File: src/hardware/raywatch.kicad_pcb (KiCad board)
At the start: 2 copper layers, 388 parts, among them J1 Conn_01x02_Pin, J10 Conn_01x04_Pin, J11 Conn_01x04_Pin, J12 Conn_01x02_Pin, J13 Conn_01x02_Pin, J14 Conn_02x08_Top_Bottom, J15 Conn_02x08_Top_Bottom, J16 Conn_02x08_Top_Bottom, J17 Conn_02x08_Top_Bottom, J18 Conn_01x02_Pin, J19 Conn_01x02_Pin, J2 Conn_01x02_Pin, J20 Conn_01x02_Pin, J21 Conn_02x08_Top_Bottom, J22 Conn_01x02_Pin, J23 Conn_01x04_Pin, J24 Conn_01x02_Pin, J25 Conn_01x02_Pin, J26 Conn_01x02_Pin, J27 Conn_01x01_Pin, J28 Conn_01x01_Pin, J29 Conn_01x02_Pin, J3 Conn_01x02_Pin, J30 Conn_01x04_Pin, J31 Conn_01x04_Pin, J32 Conn_01x01_Pin, J33 Conn_01x01_Pin, J34 046809612110846+, J35 Conn_01x02_Pin, J36 Conn_01x02_Pin, J37 Conn_01x02_Pin, J38 Conn_01x02_Pin, J39 Conn_01x02_Pin, J4 Conn_01x02_Pin, J40 Conn_01x02_Pin, J41 Conn_01x02_Pin, J42 Conn_01x02_Pin, J43 Conn_01x02_Pin, J44 Conn_01x02_Pin, J45 Conn_01x02_Pin, J46 Conn_01x02_Pin, J47 Conn_01x02_Pin, J48 Conn_01x02_Pin, J49 Conn_01x02_Pin, J5 Conn_01x02_Pin, J50 Conn_01x04_Pin, J51 MSD-1-A, J52 Conn_01x02_Pin, J53 Conn_01x02_Pin, J54 Conn_01x01_Pin, J55 Conn_01x02_Pin, J56 Conn_01x02_Pin, J57 Conn_01x02_Pin, J58 Conn_01x02_Pin, J59 Conn_01x02_Pin, J6 Conn_01x04_Pin, J60 Conn_01x02_Pin, J61 Conn_01x02_Pin, J62 Conn_01x01_Pin, J63 Conn_01x02_Pin, J64 Conn_01x02_Pin, J65 Conn_01x04_Pin, J66 Conn_01x04_Pin, J67 Conn_01x02_Pin, J68 Conn_01x02_Pin, J69 Conn_01x02_Pin, J7 Conn_01x04_Pin, J70 Conn_02x08_Top_Bottom, J71 Conn_01x02_Pin, J72 Conn_01x01_Pin, J73 Conn_02x08_Top_Bottom, J74 Conn_01x02_Pin, J75 Conn_02x08_Top_Bottom, J76 BM29B0.6-2DS/2-0.35V51, J77 Conn_01x02_Pin, J78 Conn_01x02_Pin, J79 Conn_01x02_Pin, J8 Conn_01x04_Pin, J80 Conn_01x02_Pin, J81 Conn_01x04_Pin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

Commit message: Changed pin headers to vertical
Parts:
- J1: renamed from J7; footprint Connector_PinHeader_2.54mm:PinHeader_1x04_P2.54mm_Horizontal -> Connector_PinHeader_2.54mm:PinHeader_1x04_P2.54mm_Vertical
- J10: renamed from J39; footprint Connector_PinHeader_2.54mm:PinHeader_1x02_P2.54mm_Horizontal -> Connector_PinHeader_2.54mm:PinHeader_1x02_P2.54mm_Vertical
- J11: renamed from J41; footprint Connector_PinHeader_2.54mm:PinHeader_1x02_P2.54mm_Horizontal -> Connector_PinHeader_2.54mm:PinHeader_1x02_P2.54mm_Vertical
- J12: renamed from J42; footprint Connector_PinHeader_2.54mm:PinHeader_1x02_P2.54mm_Horizontal -> Connector_PinHeader_2.54mm:PinHeader_1x02_P2.54mm_Vertical
- J13: renamed from J43; footprint Connector_PinHeader_2.54mm:PinHeader_1x02_P2.54mm_Horizontal -> Connector_PinHeader_2.54mm:PinHeader_1x02_P2.54mm_Vertical
- J14: renamed from J44; footprint Connector_PinHeader_2.54mm:PinHeader_1x02_P2.54mm_Horizontal -> Connector_PinHeader_2.54mm:PinHeader_1x02_P2.54mm_Vertical
- J15: renamed from J47; footprint Connector_PinHeader_2.54mm:PinHeader_1x02_P2.54mm_Horizontal -> Connector_PinHeader_2.54mm:PinHeader_1x02_P2.54mm_Vertical
- J16: renamed from J45; footprint Connector_PinHeader_2.54mm:PinHeader_1x02_P2.54mm_Horizontal -> Connector_PinHeader_2.54mm:PinHeader_1x02_P2.54mm_Vertical
- J17: renamed from J46; footprint Connector_PinHeader_2.54mm:PinHeader_1x02_P2.54mm_Horizontal -> Connector_PinHeader_2.54mm:PinHeader_1x02_P2.54mm_Vertical
- J18: renamed from J2; footprint Connector_PinHeader_2.54mm:PinHeader_1x02_P2.54mm_Horizontal -> Connector_PinHeader_2.54mm:PinHeader_1x02_P2.54mm_Vertical
- J19: renamed from J12; footprint Connector_PinHeader_2.54mm:PinHeader_1x02_P2.54mm_Horizontal -> Connector_PinHeader_2.54mm:PinHeader_1x02_P2.54mm_Vertical
- J2: renamed from J6; footprint Connector_PinHeader_2.54mm:PinHeader_1x04_P2.54mm_Horizontal -> Connector_PinHeader_2.54mm:PinHeader_1x04_P2.54mm_Vertical
- J20: renamed from J5; footprint Connector_PinHeader_2.54mm:PinHeader_1x02_P2.54mm_Horizontal -> Connector_PinHeader_2.54mm:PinHeader_1x02_P2.54mm_Vertical
- J21: renamed from J4; footprint Connector_PinHeader_2.54mm:PinHeader_1x02_P2.54mm_Horizontal -> Connector_PinHeader_2.54mm:PinHeader_1x02_P2.54mm_Vertical
- J22: renamed from J3; footprint Connector_PinHeader_2.54mm:PinHeader_1x02_P2.54mm_Horizontal -> Connector_PinHeader_2.54mm:PinHeader_1x02_P2.54mm_Vertical
- J25: renamed from J37; footprint Connector_PinHeader_2.54mm:PinHeader_1x02_P2.54mm_Horizontal -> Connector_PinHeader_2.54mm:PinHeader_1x02_P2.54mm_Vertical
- J26: renamed from J38; footprint Connector_PinHeader_2.54mm:PinHeader_1x02_P2.54mm_Horizontal -> Connector_PinHeader_2.54mm:PinHeader_1x02_P2.54mm_Vertical
- J27: renamed from J59; footprint Connector_PinHeader_2.54mm:PinHeader_1x02_P2.54mm_Horizontal -> Connector_PinHeader_2.54mm:PinHeader_1x02_P2.54mm_Vertical
- J28: renamed from J60; footprint Connector_PinHeader_2.54mm:PinHeader_1x02_P2.54mm_Horizontal -> Connector_PinHeader_2.54mm:PinHeader_1x02_P2.54mm_Vertical
- J29: renamed from J24; footprint Connector_PinHeader_2.54mm:PinHeader_1x02_P2.54mm_Horizontal -> Connector_PinHeader_2.54mm:PinHeader_1x02_P2.54mm_Vertical
- J3: renamed from J8; footprint Connector_PinHeader_2.54mm:PinHeader_1x04_P2.54mm_Horizontal -> Connector_PinHeader_2.54mm:PinHeader_1x04_P2.54mm_Vertical
- J30: renamed from J25; footprint Connector_PinHeader_2.54mm:PinHeader_1x02_P2.54mm_Horizontal -> Connector_PinHeader_2.54mm:PinHeader_1x02_P2.54mm_Vertical
- J33: renamed from J26; footprint Connector_PinHeader_2.54mm:PinHeader_1x02_P2.54mm_Horizontal -> Connector_PinHeader_2.54mm:PinHeader_1x02_P2.54mm_Vertical
- J34: renamed from J29; footprint Connector_PinHeader_2.54mm:PinHeader_1x02_P2.54mm_Horizontal -> Connector_PinHeader_2.54mm:PinHeader_1x02_P2.54mm_Vertical
- J36: renamed from J88; footprint Connector_PinHeader_2.54mm:PinHeader_1x02_P2.54mm_Horizontal -> Connector_PinHeader_2.54mm:PinHeader_1x02_P2.54mm_Vertical
- J37: renamed from J90; footprint Connector_PinHeader_2.54mm:PinHeader_1x02_P2.54mm_Horizontal -> Connector_PinHeader_2.54mm:PinHeader_1x02_P2.54mm_Vertical
- J38: renamed from J89; footprint Connector_PinHeader_2.54mm:PinHeader_1x02_P2.54mm_Horizontal -> Connector_PinHeader_2.54mm:PinHeader_1x02_P2.54mm_Vertical
- J39: renamed from J93; footprint Connector_PinHeader_2.54mm:PinHeader_1x02_P2.54mm_Horizontal -> Connector_PinHeader_2.54mm:PinHeader_1x02_P2.54mm_Vertical
- J4: renamed from J13; footprint Connector_PinHeader_2.54mm:PinHeader_1x02_P2.54mm_Horizontal -> Connector_PinHeader_2.54mm:PinHeader_1x02_P2.54mm_Vertical
- J40: renamed from J92; footprint Connector_PinHeader_2.54mm:PinHeader_1x02_P2.54mm_Horizontal -> Connector_PinHeader_2.54mm:PinHeader_1x02_P2.54mm_Vertical
- J41: renamed from J91; footprint Connector_PinHeader_2.54mm:PinHeader_1x02_P2.54mm_Horizontal -> Connector_PinHeader_2.54mm:PinHeader_1x02_P2.54mm_Vertical
- J42: renamed from J27; footprint Connector_PinHeader_2.54mm:PinHeader_1x01_P2.54mm_Horizontal -> Connector_PinHeader_2.54mm:PinHeader_1x04_P2.54mm_Vertical
- J43: renamed from J32; footprint Connector_PinHeader_2.54mm:PinHeader_1x01_P2.54mm_Horizontal -> Connector_PinHeader_2.54mm:PinHeader_1x04_P2.54mm_Vertical
- J44: renamed from J30; footprint Connector_PinHeader_2.54mm:PinHeader_1x04_P2.54mm_Horizontal -> Connector_PinHeader_2.54mm:PinHeader_1x04_P2.54mm_Vertical
- J45: renamed from J28; footprint Connector_PinHeader_2.54mm:PinHeader_1x01_P2.54mm_Horizontal -> Connector_PinHeader_2.54mm:PinHeader_1x04_P2.54mm_Vertical
- J46: renamed from J18; footprint Connector_PinHeader_2.54mm:PinHeader_1x02_P2.54mm_Horizontal -> Connector_PinHeader_2.54mm:PinHeader_1x02_P2.54mm_Vertical
- J47: renamed from J33; footprint Connector_PinHeader_2.54mm:PinHeader_1x01_P2.54mm_Horizontal -> Connector_PinHeader_2.54mm:PinHeader_1x04_P2.54mm_Vertical
- J48: renamed from J31; footprint Connector_PinHeader_2.54mm:PinHeader_1x04_P2.54mm_Horizontal -> Connector_PinHeader_2.54mm:PinHeader_1x04_P2.54mm_Vertical
- J5: renamed from J1; footprint Connector_PinHeader_2.54mm:PinHeader_1x02_P2.54mm_Horizontal -> Connector_PinHeader_2.54mm:PinHeader_1x02_P2.54mm_Vertical
- J50: renamed from J65; footprint Connector_PinHeader_2.54mm:PinHeader_1x04_P2.54mm_Horizontal -> Connector_PinHeader_2.54mm:PinHeader_1x04_P2.54mm_Vertical
- J51: renamed from J19; footprint Connector_PinHeader_2.54mm:PinHeader_1x02_P2.54mm_Horizontal -> Connector_PinHeader_2.54mm:PinHeader_1x02_P2.54mm_Vertical
- J52: renamed from J20; footprint Connector_PinHeader_2.54mm:PinHeader_1x02_P2.54mm_Horizontal -> Connector_PinHeader_2.54mm:PinHeader_1x02_P2.54mm_Vertical
- J53: renamed from J77; footprint Connector_PinHeader_2.54mm:PinHeader_1x02_P2.54mm_Horizontal -> Connector_PinHeader_2.54mm:PinHeader_1x02_P2.54mm_Vertical
- J54: renamed from J66; footprint Connector_PinHeader_2.54mm:PinHeader_1x04_P2.54mm_Horizontal -> Connector_PinHeader_2.54mm:PinHeader_1x04_P2.54mm_Vertical
- J55: renamed from J78; footprint Connector_PinHeader_2.54mm:PinHeader_1x02_P2.54mm_Horizontal -> Connector_PinHeader_2.54mm:PinHeader_1x02_P2.54mm_Vertical
- J56: renamed from J79; footprint Connector_PinHeader_2.54mm:PinHeader_1x02_P2.54mm_Horizontal -> Connector_PinHeader_2.54mm:PinHeader_1x02_P2.54mm_Vertical
- J57: renamed from J80; footprint Connector_PinHeader_2.54mm:PinHeader_1x02_P2.54mm_Horizontal -> Connector_PinHeader_2.54mm:PinHeader_1x02_P2.54mm_Vertical
- J59: renamed from J35; footprint Connector_PinHeader_2.54mm:PinHeader_1x02_P2.54mm_Horizontal -> Connector_PinHeader_2.54mm:PinHeader_1x02_P2.54mm_Vertical
- J6: renamed from J9; footprint Connector_PinHeader_2.54mm:PinHeader_1x04_P2.54mm_Horizontal -> Connector_PinHeader_2.54mm:PinHeader_1x04_P2.54mm_Vertical
- J60: renamed from J36; footprint Connector_PinHeader_2.54mm:PinHeader_1x02_P2.54mm_Horizontal -> Connector_PinHeader_2.54mm:PinHeader_1x02_P2.54mm_Vertical
- J61: renamed from J64; footprint Connector_PinHeader_2.54mm:PinHeader_1x02_P2.54mm_Horizontal -> Connector_PinHeader_2.54mm:PinHeader_1x02_P2.54mm_Vertical
- J62: renamed from J81; footprint Connector_PinHeader_2.54mm:PinHeader_1x04_P2.54mm_Horizontal -> Connector_PinHeader_2.54mm:PinHeader_1x04_P2.54mm_Vertical
- J63: renamed from J94; footprint Connector_PinHeader_2.54mm:PinHeader_1x02_P2.54mm_Horizontal -> Connector_PinHeader_2.54mm:PinHeader_1x02_P2.54mm_Vertical
- J64: renamed from J97; footprint Connector_PinHeader_2.54mm:PinHeader_1x02_P2.54mm_Horizontal -> Connector_PinHeader_2.54mm:PinHeader_1x02_P2.54mm_Vertical
- J65: renamed from J96; footprint Connector_PinHeader_2.54mm:PinHeader_1x02_P2.54mm_Horizontal -> Connector_PinHeader_2.54mm:PinHeader_1x02_P2.54mm_Vertical
- J66: renamed from J95; footprint Connector_PinHeader_2.54mm:PinHeader_1x02_P2.54mm_Horizontal -> Connector_PinHeader_2.54mm:PinHeader_1x02_P2.54mm_Vertical
- J68: renamed from J62; footprint Connector_PinHeader_2.54mm:PinHeader_1x01_P2.54mm_Horizontal -> Connector_PinHeader_2.54mm:PinHeader_1x04_P2.54mm_Vertical
- J69: renamed from J23; footprint Connector_PinHeader_2.54mm:PinHeader_1x04_P2.54mm_Horizontal -> Connector_PinHeader_2.54mm:PinHeader_1x04_P2.54mm_Vertical
- J7: renamed from J10; footprint Connector_PinHeader_2.54mm:PinHeader_1x04_P2.54mm_Horizontal -> Connector_PinHeader_2.54mm:PinHeader_1x04_P2.54mm_Vertical
- J70: renamed from J22; footprint Connector_PinHeader_2.54mm:PinHeader_1x02_P2.54mm_Horizontal -> Connector_PinHeader_2.54mm:PinHeader_1x02_P2.54mm_Vertical
- J71: renamed from J49; footprint Connector_PinHeader_2.54mm:PinHeader_1x02_P2.54mm_Horizontal -> Connector_PinHeader_2.54mm:PinHeader_1x02_P2.54mm_Vertical
- J73: renamed from J48; footprint Connector_PinHeader_2.54mm:PinHeader_1x02_P2.54mm_Horizontal -> Connector_PinHeader_2.54mm:PinHeader_1x02_P2.54mm_Vertical
- J74: renamed from J50; footprint Connector_PinHeader_2.54mm:PinHeader_1x04_P2.54mm_Horizontal -> Connector_PinHeader_2.54mm:PinHeader_1x04_P2.54mm_Vertical
- J76: renamed from J87; footprint Connector_PinHeader_2.54mm:PinHeader_1x01_P2.54mm_Horizontal -> Connector_PinHeader_2.54mm:PinHeader_1x04_P2.54mm_Vertical
- J77: renamed from J74; footprint Connector_PinHeader_2.54mm:PinHeader_1x02_P2.54mm_Horizontal -> Connector_PinHeader_2.54mm:PinHeader_1x04_P2.54mm_Vertical
- J79: renamed from J69; footprint Connector_PinHeader_2.54mm:PinHeader_1x02_P2.54mm_Horizontal -> Connector_PinHeader_2.54mm:PinHeader_1x02_P2.54mm_Vertical
- J8: renamed from J11; footprint Connector_PinHeader_2.54mm:PinHeader_1x04_P2.54mm_Horizontal -> Connector_PinHeader_2.54mm:PinHeader_1x04_P2.54mm_Vertical
- J80: renamed from J98; footprint Connector_PinHeader_2.54mm:PinHeader_1x04_P2.54mm_Horizontal -> Connector_PinHeader_2.54mm:PinHeader_1x04_P2.54mm_Vertical
- J81: renamed from J63; footprint Connector_PinHeader_2.54mm:PinHeader_1x02_P2.54mm_Horizontal -> Connector_PinHeader_2.54mm:PinHeader_1x02_P2.54mm_Vertical
- J82: renamed from J61; footprint Connector_PinHeader_2.54mm:PinHeader_1x02_P2.54mm_Horizontal -> Connector_PinHeader_2.54mm:PinHeader_1x02_P2.54mm_Vertical
- J83: renamed from J82; footprint Connector_PinHeader_2.54mm:PinHeader_1x02_P2.54mm_Horizontal -> Connector_PinHeader_2.54mm:PinHeader_1x02_P2.54mm_Vertical
- J85: renamed from J86; footprint Connector_PinHeader_2.54mm:PinHeader_1x02_P2.54mm_Horizontal -> Connector_PinHeader_2.54mm:PinHeader_1x02_P2.54mm_Vertical
- J86: renamed from J56; footprint Connector_PinHeader_2.54mm:PinHeader_1x02_P2.54mm_Horizontal -> Connector_PinHeader_2.54mm:PinHeader_1x02_P2.54mm_Vertical
- J87: renamed from J83; footprint Connector_PinHeader_2.54mm:PinHeader_1x04_P2.54mm_Horizontal -> Connector_PinHeader_2.54mm:PinHeader_1x04_P2.54mm_Vertical
- J88: renamed from J72; footprint Connector_PinHeader_2.54mm:PinHeader_1x01_P2.54mm_Horizontal -> Connector_PinHeader_2.54mm:PinHeader_1x04_P2.54mm_Vertical
- J9: renamed from J40; footprint Connector_PinHeader_2.54mm:PinHeader_1x02_P2.54mm_Horizontal -> Connector_PinHeader_2.54mm:PinHeader_1x02_P2.54mm_Vertical
- J90: renamed from J58; footprint Connector_PinHeader_2.54mm:PinHeader_1x02_P2.54mm_Horizontal -> Connector_PinHeader_2.54mm:PinHeader_1x02_P2.54mm_Vertical
- J91: renamed from J57; footprint Connector_PinHeader_2.54mm:PinHeader_1x02_P2.54mm_Horizontal -> Connector_PinHeader_2.54mm:PinHeader_1x02_P2.54mm_Vertical
- J92: renamed from J71; footprint Connector_PinHeader_2.54mm:PinHeader_1x02_P2.54mm_Horizontal -> Connector_PinHeader_2.54mm:PinHeader_1x04_P2.54mm_Vertical
- J93: renamed from J52; footprint Connector_PinHeader_2.54mm:PinHeader_1x02_P2.54mm_Horizontal -> Connector_PinHeader_2.54mm:PinHeader_1x02_P2.54mm_Vertical
- J94: renamed from J53; footprint Connector_PinHeader_2.54mm:PinHeader_1x02_P2.54mm_Horizontal -> Connector_PinHeader_2.54mm:PinHeader_1x02_P2.54mm_Vertical
- J95: renamed from J54; footprint Connector_PinHeader_2.54mm:PinHeader_1x01_P2.54mm_Horizontal -> Connector_PinHeader_2.54mm:PinHeader_1x04_P2.54mm_Vertical
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- renumbered ANT2 to ANT1, ANT1 to ANT2, B2 to B1, B1 to B2, C32 to C1, C34 to C10, C45 to C100, C47 to C101, C41 to C102, C63 to C103, C64 to C104, C42 to C105, C44 to C106, C43 to C107, C60 to C108, C37 to C11, C36 to C12, C35 to C13, C17 to C14, C13 to C16, C7 to C17, C9 to C18, C16 to C19, C26 to C2, C14 to C20, C8 to C21, C11 to C22, C3 to C23, C10 to C24, C4 to C25, C1 to C26, C2 to C27, C5 to C28, C12 to C29, C27 to C3, C6 to C30, C48 to C31, C25 to C32, C22 to C33, C23 to C34, C94 to C35, C78 to C36, C77 to C37, C81 to C38, C90 to C39, C38 to C4, C86 to C40, C87 to C41, C89 to C42, C91 to C43, C79 to C44, C85 to C45, C88 to C46, C80 to C47, C95 to C48, C82 to C49, C28 to C5, C93 to C50, C83 to C51, C84 to C52, C92 to C53, C96 to C54, C39 to C55, C40 to C56, C24 to C57, C55 to C58, C57 to C59, C31 to C6, C51 to C60, C58 to C61, C53 to C62, C59 to C63, C54 to C64, C56 to C65, C52 to C66, C68 to C67, C67 to C68, C30 to C7, C18 to C71, C20 to C72, C19 to C73, C21 to C74, C66 to C75, C65 to C76, C61 to C77, C62 to C78, C100 to C79, C33 to C8, C101 to C80, C98 to C81, C103 to C82, C105 to C83, C107 to C84, C106 to C85, C104 to C86, C102 to C87, C97 to C88, C99 to C89, C29 to C9, C108 to C90, C49 to C91, C50 to C92, C74 to C93, C75 to C94, C72 to C95, C73 to C96, C71 to C97, C46 to C98, C76 to C99, D9 to D1, D43 to D10, D35 to D11, D50 to D12, D34 to D13, D41 to D14, D27 to D15, D26 to D16, D25 to D17, D57 to D18, D33 to D19, D1 to D2, D59 to D20, D65 to D21, D17 to D22, D19 to D23, D18 to D24, D66 to D25, D51 to D26, D42 to D27, D6 to D28, D4 to D29, D2 to D3, D13 to D30, D14 to D31, D7 to D32, D12 to D33, D5 to D34, D16 to D35, D8 to D36, D15 to D37, D39 to D38, D23 to D39, D3 to D4, D70 to D40, D24 to D41, D47 to D42, D72 to D43, D37 to D44, D30 to D45, D45 to D46, D22 to D47, D54 to D48, D21 to D49, D11 to D5, D63 to D50, D48 to D51, D32 to D52, D31 to D53, D56 to D54, D68 to D55, D52 to D56, D64 to D57, D20 to D58, D28 to D59, D10 to D6, D29 to D60, D38 to D61, D36 to D62, D46 to D63, D40 to D64, D60 to D65, D44 to D66, D71 to D67, D53 to D68, D62 to D69, D49 to D7, D61 to D70, D69 to D71, D55 to D72, D67 to D8, D58 to D9, J14 to J23, J15 to J24, J21 to J31, J17 to J32, J16 to J35, J34 to J49, J51 to J58, J76 to J67, J84 to J72, J70 to J78, J85 to J84, J73 to J89, L5 to L1, L7 to L10, L4 to L3, L6 to L4, L1 to L5, L3 to L6, L9 to L7, L10 to L8, L8 to L9, R2 to R1, R12 to R11, R11 to R12, R38 to R13, R39 to R14, R42 to R15, R41 to R16, R40 to R17, R44 to R18, R43 to R19, R8 to R2, R17 to R20, R26 to R21, R27 to R22, R30 to R23, R32 to R24, R29 to R25, R31 to R26, R28 to R27, R15 to R28, R14 to R29, R1 to R3, R16 to R30, R13 to R31, R20 to R32, R23 to R33, R18 to R34, R24 to R35, R21 to R36, R22 to R37, R19 to R38, R25 to R39, R3 to R4, R45 to R40, R34 to R41, R37 to R42, R36 to R43, R33 to R44, R35 to R45, R9 to R7, R7 to R8, R4 to R9, S2 to S1, S4 to S2, S1 to S4, U6 to U10, U5 to U11, U3 to U12, U4 to U13, U33 to U14, U34 to U15, U35 to U16, U36 to U17, U15 to U18, U7 to U19, U14 to U2, U8 to U20, U20 to U22, U22 to U24, U28 to U25, U29 to U26, U30 to U27, U32 to U28, U31 to U29, U10 to U3, U27 to U30, U25 to U31, U37 to U32, U19 to U33, U17 to U34, U26 to U35, U16 to U36, U24 to U37, U13 to U4, U11 to U5, U18 to U6, U9 to U7, U12 to U8, U2 to U9, Y3 to Y1, Y1 to Y2, Y2 to Y3
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
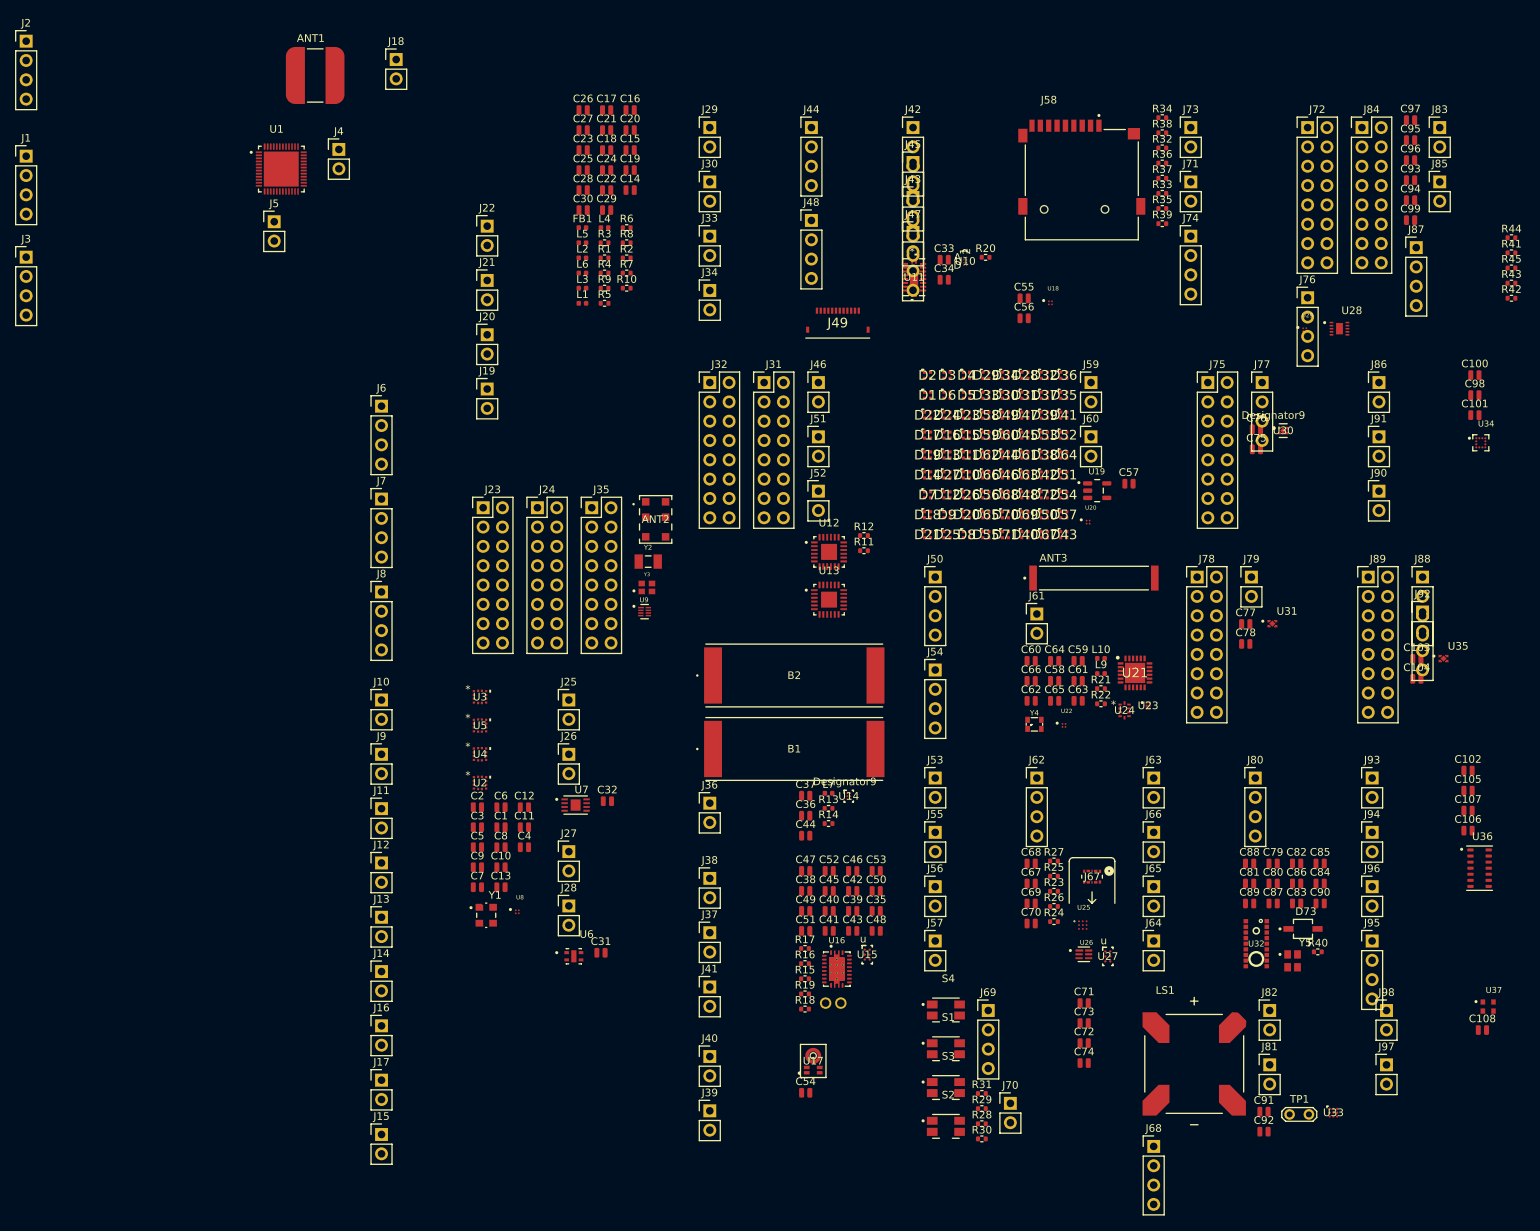
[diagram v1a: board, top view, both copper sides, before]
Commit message: Reimported footprints; Switched up some 4pin and 2pin headers
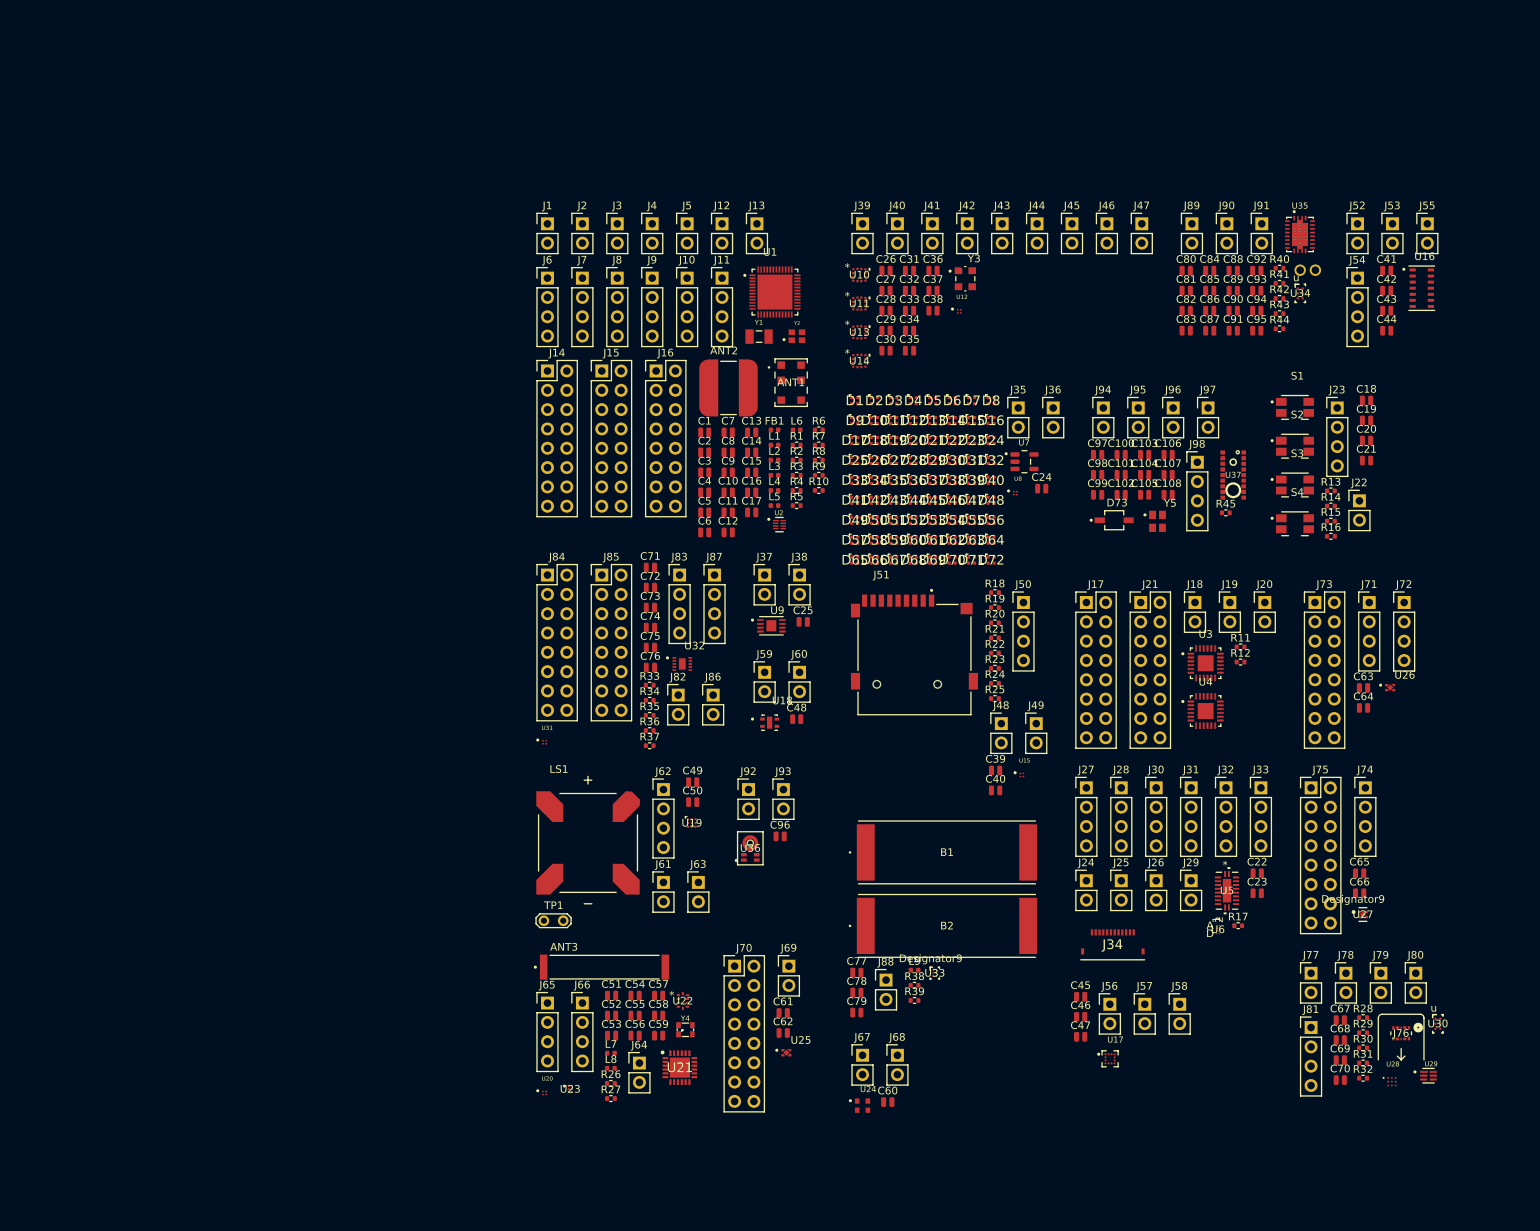
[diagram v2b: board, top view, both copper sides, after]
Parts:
- ANT1: value W3102 -> SR4W035; footprint Project:IND_W3102 -> Project:SR4W035_4X6_ANT
- ANT2: value SR4W035 -> W3102; footprint Project:SR4W035_4X6_ANT -> Project:IND_W3102
- C1, C5: value 100nF -> 1.5pF
- C10: value 10µF -> 2.2µF
- C100: value 4.7µF -> 100nF
- C101, C81, C82, C86, C96: value 1µF -> 100nF
- C106, C22, C49, C54, C62, C66: value 100nF -> 1µF
- C107: value 4.7µF -> 10µF
- C12: value 100nF -> 2.2nF
- C14: value 2.2µF -> 10nF
- C16: value 100nF -> 100pF
- C17: value 27pF -> 2.2µF
- C18: value 10µF -> 10nF
- C19: value 100pF -> 10nF
- C2: value 10µF -> 2pF
- C21: value 27pF -> 10nF
- C23: value 3.9pF -> 1µF
- C24: value 2.2µF -> 10pF
- C25: value 3pF -> 100nF
- C26: value 1.5pF -> 10µF
- C27: value 2pF -> 10µF
- C28: value 1.5pF -> 100nF
- C29: value 2.2nF -> 100nF
- C3: value 10µF -> 3.9pF
- C33, C34, C75, C76, C77, C78: value 1µF -> 10µF
- C35: value 470nF -> 100nF
- C36, C37, C44, C97, C99: value 10µF -> 100nF
- C39, C42: value 22nF -> 10µF
- C4: value 100nF -> 3pF
- C41: value 10nF -> 100nF
- C43: value 2.2nF -> 4.7µF
- C45: value 10nF -> 4.7µF
- C46, C60: value 470nF -> 1µF
- C47: value 10µF -> 1µF
- C48, C52: value 22nF -> 100nF
- C50, C72, C73, C74: value 10nF -> 1µF
- C51, C94: value 10µF -> 470nF
- C53: value 100pF -> 100nF
- C55: value 10µF -> 10pF
- C56: value 100nF -> 47nF
- C57: value 10pF -> 47pF
- C58: value 10pF -> 1nF
- C59: value 47pF -> 39pF
- C61: value 1nF -> 1µF
- C63: value 39pF -> 1µF
- C65: value 47nF -> 1µF
- C67: value 100µF -> 1µF
- C68: value 1µF -> 100µF
- C7: value 100nF -> 27pF
- C71: value 10nF -> 10µF
- C79, C80, C9: value 100nF -> 10µF
- C8: value 10µF -> 27pF
- C84: value 10µF -> 22nF
- C85, C93: value 1µF -> 10nF
- C87: value 100nF -> 10nF
- C88: value 100nF -> 470nF
- C89: value 100nF -> 22nF
- C90, C95: value 1µF -> 22nF
- C91: value 1µF -> 2.2nF
- C92: value 1µF -> 100pF
- J1, J2, J3, J44, J48, J69, J80: value Conn_01x04_Pin -> Conn_01x02_Pin; footprint Connector_PinHeader_2.54mm:PinHeader_1x04_P2.54mm_Vertical -> Connector_PinHeader_2.54mm:PinHeader_1x02_P2.54mm_Vertical
- J10, J11, J30, J65, J66, J81, J83, J9, J98: value Conn_01x02_Pin -> Conn_01x04_Pin; footprint Connector_PinHeader_2.54mm:PinHeader_1x02_P2.54mm_Vertical -> Connector_PinHeader_2.54mm:PinHeader_1x04_P2.54mm_Vertical
- J14, J15, J16, J17, J21, J70, J73, J85: value Conn_01x02_Pin -> Conn_02x08_Top_Bottom; footprint Connector_PinHeader_2.54mm:PinHeader_1x02_P2.54mm_Vertical -> Connector_PinHeader_2.54mm:PinHeader_2x08_P2.54mm_Vertical
- J23, J31: value Conn_02x08_Top_Bottom -> Conn_01x04_Pin; footprint Connector_PinHeader_2.54mm:PinHeader_2x08_P2.54mm_Vertical -> Connector_PinHeader_2.54mm:PinHeader_1x04_P2.54mm_Vertical
- J24, J35, J78, J89: value Conn_02x08_Top_Bottom -> Conn_01x02_Pin; footprint Connector_PinHeader_2.54mm:PinHeader_2x08_P2.54mm_Vertical -> Connector_PinHeader_2.54mm:PinHeader_1x02_P2.54mm_Vertical
- J27, J28, J33: value Conn_01x02_Pin -> Conn_01x01_Pin; footprint Connector_PinHeader_2.54mm:PinHeader_1x02_P2.54mm_Vertical -> Connector_PinHeader_2.54mm:PinHeader_1x04_P2.54mm_Vertical
- J32, J72: value Conn_02x08_Top_Bottom -> Conn_01x01_Pin; footprint Connector_PinHeader_2.54mm:PinHeader_2x08_P2.54mm_Vertical -> Connector_PinHeader_2.54mm:PinHeader_1x04_P2.54mm_Vertical
- J34: value Conn_01x02_Pin -> 046809612110846+; footprint Connector_PinHeader_2.54mm:PinHeader_1x02_P2.54mm_Vertical -> Project:046809612110846
- J42, J43, J45, J47, J68, J88, J95: value Conn_01x01_Pin -> Conn_01x02_Pin; footprint Connector_PinHeader_2.54mm:PinHeader_1x04_P2.54mm_Vertical -> Connector_PinHeader_2.54mm:PinHeader_1x02_P2.54mm_Vertical
- J49: value 046809612110846+ -> Conn_01x02_Pin; footprint Project:046809612110846 -> Connector_PinHeader_2.54mm:PinHeader_1x02_P2.54mm_Vertical
- J51: value Conn_01x02_Pin -> MSD-1-A; footprint Connector_PinHeader_2.54mm:PinHeader_1x02_P2.54mm_Vertical -> Project:CUI_MSD-1-A
- J54, J62, J87: value Conn_01x04_Pin -> Conn_01x01_Pin
- J58: value MSD-1-A -> Conn_01x02_Pin; footprint Project:CUI_MSD-1-A -> Connector_PinHeader_2.54mm:PinHeader_1x02_P2.54mm_Vertical
- J67: value BM29B0.6-2DS/2-0.35V51 -> Conn_01x02_Pin; footprint Project:CONN_BM29B0.6-2DS&slash_2-0.35V51_HIR -> Connector_PinHeader_2.54mm:PinHeader_1x02_P2.54mm_Vertical
- J71: footprint Connector_PinHeader_2.54mm:PinHeader_1x02_P2.54mm_Vertical -> Connector_PinHeader_2.54mm:PinHeader_1x04_P2.54mm_Vertical
- J74: value Conn_01x04_Pin -> Conn_01x02_Pin
- J76: value Conn_01x01_Pin -> BM29B0.6-2DS/2-0.35V51; footprint Connector_PinHeader_2.54mm:PinHeader_1x04_P2.54mm_Vertical -> Project:CONN_BM29B0.6-2DS&slash_2-0.35V51_HIR
- J77, J92: footprint Connector_PinHeader_2.54mm:PinHeader_1x04_P2.54mm_Vertical -> Connector_PinHeader_2.54mm:PinHeader_1x02_P2.54mm_Vertical
- L1: value 2.2nH -> 2.7nH
- L10: value 10µH -> WE-WPCC_RX_1COIL; footprint Inductor_SMD:L_0402_1005Metric -> Project:WE-WPCC_RX_760308103205
- L3: value - -> 2.5nH
- L4: value 4.7µH -> -
- L5: value 2.7nH -> 2.2nH
- L6: value 2.5nH -> 4.7µH
- L7: value 2.2µH -> 10µH
- L8: value WE-WPCC_RX_1COIL -> 47nH; footprint Project:WE-WPCC_RX_760308103205 -> Inductor_SMD:L_0402_1005Metric
- L9: value 47nH -> 2.2µH
- R13: value 400KΩ -> 200kΩ
- R14: value 100KΩ -> 200kΩ
- R15: value 422Ω -> 200kΩ
- R16: value 10kΩ -> 200kΩ
- R17: value 200Ω -> 10kΩ
- R18, R19: value 10kΩ -> 28Ω
- R2: value 10kΩ -> 1kΩ
- R21: value 100Ω -> 10kΩ
- R22: value 220Ω -> 10kΩ
- R24: value 10mΩ -> 28Ω
- R26: value 2.2kΩ -> 100Ω
- R27: value 330Ω -> 220Ω
- R28: value 200kΩ -> 330Ω
- R29, R30: value 200kΩ -> 10kΩ
- R3: value 1kΩ -> 200kΩ
- R31: value 200kΩ -> 2.2kΩ
- R32: value 10kΩ -> 10mΩ
- R33: value 10kΩ -> 43kΩ
- R34, R35: value 28Ω -> 10kΩ
- R36, R37: value 10kΩ -> 2.2kΩ
- R38: value 28Ω -> 400KΩ
- R39: value 10kΩ -> 100KΩ
- R4: value 200kΩ -> 100kΩ
- R40: value 10kΩ -> 200Ω
- R42: value 2.2kΩ -> 422Ω
- R43: value 2.2kΩ -> 10kΩ
- R44: value 43kΩ -> 10kΩ
- R9: value 100kΩ -> 10kΩ
- U10: value LP5817YCHR -> LIS2DUX12TR; footprint Project:DSBGA-8_YCH0008_TEX -> Project:LGA-12_2.0X2.0X0.74_LIS2DUX12_STM
- U11: value TXS0108ERKSR -> LIS2DUX12TR; footprint Project:VQFN20_RKS_TEX -> Project:LGA-12_2.0X2.0X0.74_LIS2DUX12_STM
- U12: value PCAL6416AHF_128 -> TPS22916BYFPR; footprint Project:QFN50P400X400X80-25N -> Project:IC_TPS22916BYFPR
- U13: value PCAL6416AHF_128 -> LIS2DUX12TR; footprint Project:QFN50P400X400X80-25N -> Project:LGA-12_2.0X2.0X0.74_LIS2DUX12_STM
- U14: value TPS61099YFFT -> LIS2DUX12TR; footprint Project:YFF0006AFAD -> Project:LGA-12_2.0X2.0X0.74_LIS2DUX12_STM
- U15: value CSD83325L -> TPS22916BYFPR; footprint Project:YJE0006A -> Project:IC_TPS22916BYFPR
- U16: value BQ51013BRHLR -> MAX30101EFD_T; footprint Project:IC_MSP430FR2522IRHLR -> Project:PSON80P560X330X165-14N
- U17: value IM72D128V01XTMA1 -> MMC34160PJ; footprint Project:PG-LLGA-5-3_INF -> Project:XDCR_MMC34160PJ
- U18: value TPS22916BYFPR -> ENS210-LQFM; footprint Project:IC_TPS22916BYFPR -> Project:XDCR_ENS210-LQFM
- U19: value SN74AHCT1G125DBVR -> DRV2605LYZFR; footprint Project:SOT95P280X145-5N -> Project:YZF0009ADAD
- U2: value LIS2DUX12TR -> PCA9306DQER; footprint Project:LGA-12_2.0X2.0X0.74_LIS2DUX12_STM -> Project:SON35P140X100X40-8N
- U22: value TPS22916BYFPR -> 0900FM15K0039001E; footprint Project:IC_TPS22916BYFPR -> Project:QFP20P0X0X31-0_JOT
- U24: value 0900FM15K0039001E -> LTR-329ALS-01; footprint Project:QFP20P0X0X31-0_JOT -> Project:IC_LTR-329ALS-01
- U25: value BQ27426YZFR -> TPS7A2018PDQNR; footprint Project:IC_BQ27421YZFR-G1A -> Project:VREG_TPS7A2018PDQNR
- U26: value BQ29700DSER -> TPS7A2030PDQNR; footprint Project:SON50P150X150X80-6N -> Project:VREG_TPS7A2030PDQNR
- U27: value CSD83325L -> TPS7A2033DQNR; footprint Project:YJE0006A -> Project:DQN0004A-MFG
- U28: value BQ25185DLHR -> BQ27426YZFR; footprint Project:IC_BQ25185DLHR -> Project:IC_BQ27421YZFR-G1A
- U29: value TPS22916BYFPR -> BQ29700DSER; footprint Project:IC_TPS22916BYFPR -> Project:SON50P150X150X80-6N
- U3, U4: value LIS2DUX12TR -> PCAL6416AHF_128; footprint Project:LGA-12_2.0X2.0X0.74_LIS2DUX12_STM -> Project:QFN50P400X400X80-25N
- U30: value TPS7A2033DQNR -> CSD83325L; footprint Project:DQN0004A-MFG -> Project:YJE0006A
- U31: value TPS7A2018PDQNR -> TPS22916BYFPR; footprint Project:VREG_TPS7A2018PDQNR -> Project:IC_TPS22916BYFPR
- U32: value APDS-9500 -> BQ25185DLHR; footprint Project:ADPS-9500 -> Project:IC_BQ25185DLHR
- U33: value DRV2605LYZFR -> TPS61099YFFT; footprint Project:YZF0009ADAD -> Project:YFF0006AFAD
- U34: value MMC34160PJ -> CSD83325L; footprint Project:XDCR_MMC34160PJ -> Project:YJE0006A
- U35: value TPS7A2030PDQNR -> BQ51013BRHLR; footprint Project:VREG_TPS7A2030PDQNR -> Project:IC_MSP430FR2522IRHLR
- U36: value MAX30101EFD_T -> IM72D128V01XTMA1; footprint Project:PSON80P560X330X165-14N -> Project:PG-LLGA-5-3_INF
- U37: value LTR-329ALS-01 -> APDS-9500; footprint Project:IC_LTR-329ALS-01 -> Project:ADPS-9500
- U5: value LIS2DUX12TR -> TXS0108ERKSR; footprint Project:LGA-12_2.0X2.0X0.74_LIS2DUX12_STM -> Project:VQFN20_RKS_TEX
- U6: value ENS210-LQFM -> LP5817YCHR; footprint Project:XDCR_ENS210-LQFM -> Project:DSBGA-8_YCH0008_TEX
- U7: value ATECC608A-MAHDA-S -> SN74AHCT1G125DBVR; footprint Project:SON50P200X300X60-9N -> Project:SOT95P280X145-5N
- U9: value PCA9306DQER -> ATECC608A-MAHDA-S; footprint Project:SON35P140X100X40-8N -> Project:SON50P200X300X60-9N
- Y1: value DSC6003CE2A -> ABS07-32.768KHZ-7-T; footprint Project:OSC_DSC6003CE2A-000.0000 -> Project:XTAL_ABS07-32.768KHZ-7-T
- Y2: value ABS07-32.768KHZ-7-T -> ECS-320-8-37B-CKY-TR; footprint Project:XTAL_ABS07-32.768KHZ-7-T -> Project:XTAL_ECS-160-9-37-CKM-TR
- Y3: value ECS-320-8-37B-CKY-TR -> DSC6003CE2A; footprint Project:XTAL_ECS-160-9-37-CKM-TR -> Project:OSC_DSC6003CE2A-000.0000
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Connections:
- ANT1 pad 1: /MC: Microcontroller/NFC1 -> unconnected-(ANT1-NC-Pad1)
- ANT1 pad 2: /MC: Microcontroller/NFC2 -> Net-(ANT1-FEED)
- ANT2 pad 1: unconnected-(ANT1-NC-Pad1) -> /MC: Microcontroller/NFC1
- ANT2 pad 2: Net-(ANT1-FEED) -> /MC: Microcontroller/NFC2
- C1 pad 1: +3V3 -> Net-(C1-Pad1)
- C1 pad 2: GND -> /MC: Microcontroller/VSSPA
- C10 pad 1: GND -> Net-(U1-DECD)
- C10 pad 2: +1V8 -> GND
- C100 pad 1: Net-(U17-CAP) -> Net-(U37-VDDA_I/O)
- C101 pad 1: +1V8 -> +3V3
- C102 pad 1: +4V5 -> Net-(U37-VDDAY_I/O)
- C103 pad 1: +4V5 -> +3V3
- C104 pad 1: +3V0 -> Net-(U37-VDDA18_I/O)
- C106 pad 1: +1V8 -> +4V5
- C107 pad 1: +1V8 -> +4V5
- C108 pad 1: +3V3 -> +4V5
- C11 pad 2: +1V8 -> +3V3
- C12 pad 1: +3V3 -> Net-(U1-DECA)
- C13 pad 2: +1V8 -> +3V3
- C16 pad 1: GND -> Net-(U2-EN)
- C16 pad 2: +3V3 -> GND
- C17 pad 1: GND -> Net-(U1-DECA)
- C17 pad 2: /MC: Microcontroller/NFC1 -> GND
- C18 pad 1: +3V3 -> /Buttons/BTN1
- C18 pad 2: GND -> +3V3
- C19 pad 1: Net-(U2-EN) -> /Buttons/BTN2
- C19 pad 2: GND -> +3V3
- C2 pad 1: GND -> Net-(C2-Pad1)
- C2 pad 2: +1V8 -> GND
- C20 pad 1: Net-(U1-DECA) -> /Buttons/BTN3
- C20 pad 2: GND -> +3V3
- C21 pad 1: /MC: Microcontroller/NFC2 -> /Buttons/BTN4
- C21 pad 2: GND -> +3V3
- C22 pad 1: GND -> +3V3
- C22 pad 2: +3V3 -> GND
- C23 pad 1: GND -> +3V0
- C23 pad 2: Net-(U1-~{RESET}) -> GND
- C24 pad 1: Net-(U1-DECD) -> LED4V5
- C25 pad 1: Net-(C4-Pad1) -> +3V3
- C26 pad 1: Net-(C1-Pad1) -> GND
- C26 pad 2: /MC: Microcontroller/VSSPA -> +1V8
- C27 pad 1: Net-(C2-Pad1) -> GND
- C27 pad 2: GND -> +1V8
- C28 pad 1: Net-(C4-Pad1) -> Net-(U12-VOUT)
- C28 pad 2: Net-(ANT1-FEED) -> GND
- C29 pad 1: Net-(U1-DECA) -> GND
- C29 pad 2: GND -> +1V8
- C3 pad 2: +1V8 -> Net-(U1-~{RESET})
- C31 pad 1: +1V8 -> GND
- C31 pad 2: GND -> +1V8
- C33 pad 1: +3V3 -> GND
- C33 pad 2: GND -> +1V8
- C34 pad 1: +3V0 -> GND
- C34 pad 2: GND -> +1V8
- C35 pad 1: /Wireless Charging/CLAMP2 -> GND
- C35 pad 2: /Wireless Charging/AC2 -> +1V8
- C36 pad 1: VSOLAR -> +3V3
- C37 pad 1: Net-(U33-EN) -> GND
- C37 pad 2: GND -> +1V8
- C38 pad 1: GND -> +3V3
- C38 pad 2: VSOLAR -> GND
- C39 pad 1: /Wireless Charging/AC1 -> /microSD/MSD3V3
- C39 pad 2: Net-(C84-Pad2) -> GND
- C4 pad 1: +3V3 -> Net-(C4-Pad1)
- C40 pad 1: /Wireless Charging/AC1 -> /microSD/MSD3V3
- C40 pad 2: Net-(C84-Pad2) -> GND
- C41 pad 1: /Wireless Charging/BOOT1 -> +4V5
- C41 pad 2: /Wireless Charging/AC1 -> GND
- C42 pad 1: /Wireless Charging/COMM1 -> +4V5
- C42 pad 2: /Wireless Charging/AC1 -> GND
- C43 pad 1: /Wireless Charging/AC1 -> +1V8
- C43 pad 2: /Wireless Charging/AC2 -> GND
- C44 pad 1: VSOLAR -> +1V8
- C45 pad 1: /Wireless Charging/AC1 -> Net-(U17-CAP)
- C45 pad 2: Net-(C84-Pad2) -> GND
- C46 pad 1: /Wireless Charging/CLAMP1 -> +3V3
- C46 pad 2: /Wireless Charging/AC1 -> GND
- C47 pad 1: GND -> +1V8
- C47 pad 2: VSOLAR -> GND
- C48 pad 1: /Wireless Charging/COMM2 -> +1V8
- C48 pad 2: /Wireless Charging/AC2 -> GND
- C49 pad 1: VIN -> Net-(U19-REG)
- C5 pad 1: Net-(U12-VOUT) -> Net-(C4-Pad1)
- C5 pad 2: GND -> Net-(ANT1-FEED)
- C50 pad 1: /Wireless Charging/BOOT2 -> +4V5
- C50 pad 2: /Wireless Charging/AC2 -> GND
- C51 pad 1: VIN -> GND
- C51 pad 2: GND -> Net-(U21-VREG)
- C52 pad 1: /Wireless Charging/AC1 -> /LoRa/LORA3V3
- C52 pad 2: Net-(C84-Pad2) -> GND
- C53 pad 1: /Wireless Charging/AC1 -> GND
- C53 pad 2: /Wireless Charging/AC2 -> Net-(U21-DIO3)
- C54 pad 1: +3V3 -> /LoRa/LORA3V3
- C55 pad 1: /microSD/MSD3V3 -> Net-(C55-Pad1)
- C55 pad 2: GND -> Net-(U21-XTA)
- C56 pad 1: /microSD/MSD3V3 -> GND
- C56 pad 2: GND -> Net-(U21-VR_PA)
- C57 pad 1: LED4V5 -> GND
- C57 pad 2: GND -> Net-(U21-VR_PA)
- C58 pad 1: Net-(C55-Pad1) -> GND
- C58 pad 2: Net-(U21-XTA) -> /LoRa/CTRL
- C59 pad 1: GND -> Net-(ANT3-Pad1)
- C59 pad 2: Net-(U21-VR_PA) -> Net-(U23-RFIN)
- C6 pad 1: GND -> +3V3
- C6 pad 2: +1V8 -> GND
- C60 pad 1: GND -> +3V3
- C60 pad 2: Net-(U21-VREG) -> GND
- C61 pad 1: GND -> +4V5
- C61 pad 2: /LoRa/CTRL -> GND
- C62 pad 1: GND -> +1V8
- C62 pad 2: Net-(U21-DIO3) -> GND
- C63 pad 1: Net-(ANT3-Pad1) -> +4V5
- C63 pad 2: Net-(U23-RFIN) -> GND
- C64 pad 1: /LoRa/LORA3V3 -> +3V0
- C65 pad 1: GND -> +4V5
- C65 pad 2: Net-(U21-VR_PA) -> GND
- C66 pad 1: /LoRa/LORA3V3 -> +3V3
- C67 pad 1: Net-(U29-BAT) -> GND
- C67 pad 2: -BATT -> +BATT
- C68 pad 1: GND -> Net-(U29-BAT)
- C68 pad 2: +BATT -> -BATT
- C7 pad 1: +3V3 -> GND
- C7 pad 2: GND -> /MC: Microcontroller/NFC1
- C71 pad 1: /Buttons/BTN1 -> GND
- C71 pad 2: +3V3 -> VIN
- C72 pad 1: /Buttons/BTN3 -> GND
- C72 pad 2: +3V3 -> VIN
- C73 pad 1: /Buttons/BTN2 -> GND
- C73 pad 2: +3V3 -> +4V5
- C74 pad 1: /Buttons/BTN4 -> GND
- C74 pad 2: +3V3 -> VBAT
- C75 pad 1: +3V3 -> GND
- C75 pad 2: GND -> +4V5
- C76 pad 1: +4V5 -> GND
- C76 pad 2: GND -> VBAT
- C77 pad 1: +4V5 -> Net-(U33-EN)
- C78 pad 1: +1V8 -> VSOLAR
- C79 pad 1: Net-(U37-VDDA_I/O) -> VSOLAR
- C8 pad 1: GND -> /MC: Microcontroller/NFC2
- C8 pad 2: +1V8 -> GND
- C80 pad 1: +3V3 -> GND
- C80 pad 2: GND -> VSOLAR
- C81 pad 1: +3V3 -> GND
- C81 pad 2: GND -> VSOLAR
- C82 pad 1: +3V3 -> VIN
- C83 pad 1: +4V5 -> VIN
- C84 pad 1: +4V5 -> /Wireless Charging/AC1
- C84 pad 2: GND -> Net-(C84-Pad2)
- C85 pad 1: +4V5 -> /Wireless Charging/AC1
- C85 pad 2: GND -> Net-(C84-Pad2)
- C86 pad 1: Net-(U37-VDDA18_I/O) -> /Wireless Charging/AC1
- C86 pad 2: GND -> Net-(C84-Pad2)
- C87 pad 1: Net-(U37-VDDAY_I/O) -> /Wireless Charging/BOOT1
- C87 pad 2: GND -> /Wireless Charging/AC1
- C88 pad 1: +3V3 -> /Wireless Charging/CLAMP1
- C88 pad 2: GND -> /Wireless Charging/AC1
- C89 pad 1: +3V3 -> /Wireless Charging/COMM1
- C89 pad 2: GND -> /Wireless Charging/AC1
- C9 pad 1: GND -> +3V3
- C9 pad 2: +1V8 -> GND
- C90 pad 1: +4V5 -> /Wireless Charging/AC1
- C90 pad 2: GND -> Net-(C84-Pad2)
- C91 pad 1: Net-(U19-REG) -> /Wireless Charging/AC1
- C91 pad 2: GND -> /Wireless Charging/AC2
- C92 pad 1: +4V5 -> /Wireless Charging/AC1
- C92 pad 2: GND -> /Wireless Charging/AC2
- C93 pad 1: GND -> /Wireless Charging/BOOT2
- C93 pad 2: VBAT -> /Wireless Charging/AC2
- C94 pad 1: GND -> /Wireless Charging/CLAMP2
- C94 pad 2: +4V5 -> /Wireless Charging/AC2
- C95 pad 1: GND -> /Wireless Charging/COMM2
- C95 pad 2: VIN -> /Wireless Charging/AC2
- C96 pad 1: GND -> +3V3
- C96 pad 2: +4V5 -> GND
- C97 pad 1: GND -> +3V3
- C97 pad 2: VIN -> GND
- C99 pad 1: GND -> +3V3
- C99 pad 2: VBAT -> GND
- D1 pad 2: Net-(D15-DI) -> Net-(D1-DO)
- D1 pad 4: Net-(D3-DO) -> /LEDs/LEDDI4V5
- D10 pad 2: Net-(D43-DO) -> Net-(D10-DO)
- D10 pad 4: Net-(D37-DO) -> Net-(D10-DI)
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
